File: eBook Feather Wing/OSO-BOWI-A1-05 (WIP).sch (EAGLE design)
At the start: 97 parts, among them IC1 MCP23008/SO, IC2 23K256-I/SN, J1 SJ-43514-SMT, Q1 IRLML0100, SW1 SPDT_SWITCH

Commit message: wing: new footprint for inductor
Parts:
- L1: device microbuilder:INDUCTORNR401 -> Adafruit 3.5in 480x320 FeatherWing:MICROBUILDER_INDUCTORNR401_BIGPADS
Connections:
- net +3V3: now also L1.1; no longer L1.2
- net N$3: now also L1.2; no longer L1.1
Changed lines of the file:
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@@
 <part name="C9" library="microbuilder" deviceset="CAP_CERAMIC" device="0805-NOOUTLINE" value="4.7uF/25V"/>
 <part name="D3" library="microbuilder" deviceset="DIODE-SCHOTTKY" device="SOD-123" value="MBR0530"/>
-<part name="L1" library="microbuilder" deviceset="INDUCTOR" device="NR401" value="10uH"/>
 <part name="R5" library="microbuilder" deviceset="RESISTOR" device="0805_10MGAP" value="0.47ohm"/>
 <part name="U$10" library="microbuilder" deviceset="GND" device=""/>
@@
 <part name="BTN_RESET" library="adafruit" deviceset="SWITCH_PUSHBUTTON" device="C&amp;K_KSS"/>
 <part name="BTN_LOCK" library="adafruit" deviceset="SWITCH_PUSHBUTTON" device="C&amp;K_KSS"/>
+<part name="L1" library="Adafruit 3.5in 480x320 FeatherWing" deviceset="MICROBUILDER_INDUCTOR" device="NR401_BIGPADS" value="10uH"/>
 </parts>
 <sheets>
@@
 <attribute name="VALUE" x="104.1" y="144.78" size="1.27" layer="96" rot="MR270" align="center"/>
 </instance>
-<instance part="L1" gate="G$1" x="83.82" y="149.86" smashed="yes" rot="MR0">
-<attribute name="NAME" x="83.82" y="152.4" size="1.27" layer="95" rot="MR0" align="center"/>
-<attribute name="VALUE" x="83.82" y="148.32" size="1.27" layer="96" rot="MR0" align="center"/>
-</instance>
 <instance part="R5" gate="G$1" x="91.44" y="121.92" smashed="yes" rot="MR270">
 <attribute name="NAME" x="88.9" y="121.92" size="1.27" layer="95" font="vector" rot="MR270" align="center"/>
@@
 <attribute name="NAME" x="233.68" y="105.156" size="1.27" layer="95"/>
 <attribute name="VALUE" x="233.68" y="99.314" size="1.27" layer="96"/>
+</instance>
+<instance part="L1" gate="G$1" x="83.82" y="149.86" smashed="yes">
+<attribute name="NAME" x="83.82" y="152.4" size="1.27" layer="95" align="center"/>
+<attribute name="VALUE" x="83.82" y="148.32" size="1.27" layer="96" align="center"/>
 </instance>
 </instances>
@@
 </segment>
 <segment>
-<pinref part="L1" gate="G$1" pin="2"/>
 <wire x1="76.2" y1="154.94" x2="76.2" y2="149.86" width="0.1524" layer="91"/>
 <wire x1="76.2" y1="149.86" x2="78.74" y2="149.86" width="0.1524" layer="91"/>
 <pinref part="+3V7" gate="G$1" pin="+3V3"/>
+<pinref part="L1" gate="G$1" pin="1"/>
 </segment>
 <segment>
@@
 <wire x1="91.44" y1="149.86" x2="101.6" y2="149.86" width="0.1524" layer="91"/>
 <wire x1="101.6" y1="149.86" x2="101.6" y2="147.32" width="0.1524" layer="91"/>
-<pinref part="L1" gate="G$1" pin="1"/>
 <wire x1="91.44" y1="149.86" x2="88.9" y2="149.86" width="0.1524" layer="91"/>
 <junction x="91.44" y="149.86"/>
@@
 <pinref part="C9" gate="G$1" pin="1"/>
 <wire x1="114.3" y1="149.86" x2="114.3" y2="144.78" width="0.1524" layer="91"/>
-</segment>
-</net>
+<pinref part="L1" gate="G$1" pin="2"/>
+</segment>
+</net>

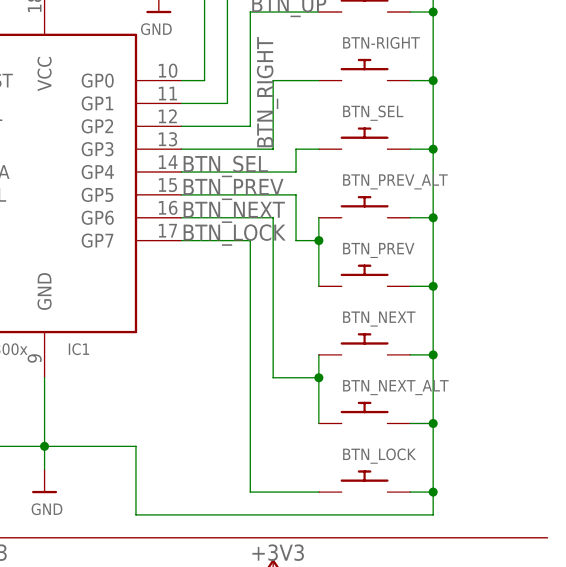
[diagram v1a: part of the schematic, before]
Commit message: rename alt buttons DNP
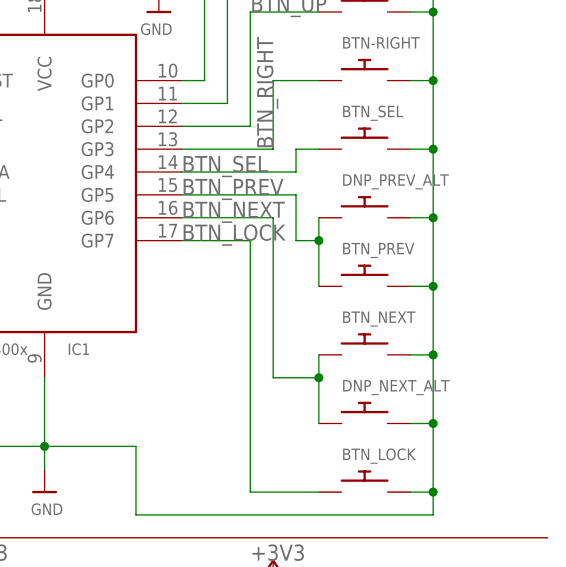
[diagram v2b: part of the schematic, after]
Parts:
- renumbered BTN_NEXT_ALT to DNP_NEXT_ALT, BTN_PREV_ALT to DNP_PREV_ALT
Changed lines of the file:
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@@
 <part name="U$16" library="microbuilder" deviceset="GND" device=""/>
 <part name="U$12" library="microbuilder" deviceset="GND" device=""/>
-<part name="BTN_PREV_ALT" library="My Stuff" deviceset="SPST_TACTILE_SWITCH" device="RA"/>
+<part name="DNP_PREV_ALT" library="My Stuff" deviceset="SPST_TACTILE_SWITCH" device="RA"/>
 <part name="+3V6" library="supply1" library_urn="urn:adsk.eagle:library:371" deviceset="+3V3" device=""/>
 <part name="R4" library="microbuilder" deviceset="RESISTOR" device="_0805MP" value="10K"/>
@@
 <part name="INT" library="Adafruit 3.5in 480x320 FeatherWing" deviceset="MICROBUILDER_SOLDERJUMPER_CLOSED" device=""/>
 <part name="C5" library="microbuilder" deviceset="CAP_CERAMIC" device="0805_10MGAP" value="1uF"/>
-<part name="BTN_NEXT_ALT" library="My Stuff" deviceset="SPST_TACTILE_SWITCH" device="RA"/>
+<part name="DNP_NEXT_ALT" library="My Stuff" deviceset="SPST_TACTILE_SWITCH" device="RA"/>
 <part name="ERST" library="Adafruit 3.5in 480x320 FeatherWing" deviceset="MICROBUILDER_SOLDERJUMPER_CLOSED" device=""/>
 <part name="EBSY" library="Adafruit 3.5in 480x320 FeatherWing" deviceset="MICROBUILDER_SOLDERJUMPER_CLOSED" device=""/>
@@
 <attribute name="VALUE" x="252.984" y="27.94" size="1.27" layer="96" rot="MR0"/>
 </instance>
-<instance part="BTN_PREV_ALT" gate="G$1" x="236.22" y="132.08" smashed="yes">
+<instance part="DNP_PREV_ALT" gate="G$1" x="236.22" y="132.08" smashed="yes">
 <attribute name="NAME" x="233.68" y="135.636" size="1.27" layer="95"/>
 </instance>
@@
 <attribute name="VALUE" x="177.56" y="118.09" size="1.27" layer="96" font="vector" rot="R90" align="center"/>
 </instance>
-<instance part="BTN_NEXT_ALT" gate="G$1" x="236.22" y="109.22" smashed="yes">
+<instance part="DNP_NEXT_ALT" gate="G$1" x="236.22" y="109.22" smashed="yes">
 <attribute name="NAME" x="233.68" y="112.776" size="1.27" layer="95"/>
 </instance>
@@
 <junction x="243.84" y="139.7"/>
 <wire x1="243.84" y1="132.08" x2="243.84" y2="139.7" width="0.1524" layer="91"/>
-<pinref part="BTN_PREV_ALT" gate="G$1" pin="P$2"/>
+<pinref part="DNP_PREV_ALT" gate="G$1" pin="P$2"/>
 <wire x1="241.3" y1="132.08" x2="243.84" y2="132.08" width="0.1524" layer="91"/>
 <junction x="243.84" y="132.08"/>
@@
 <junction x="243.84" y="116.84"/>
 <wire x1="243.84" y1="109.22" x2="243.84" y2="116.84" width="0.1524" layer="91"/>
-<pinref part="BTN_NEXT_ALT" gate="G$1" pin="P$2"/>
+<pinref part="DNP_NEXT_ALT" gate="G$1" pin="P$2"/>
 <wire x1="241.3" y1="109.22" x2="243.84" y2="109.22" width="0.1524" layer="91"/>
 <wire x1="241.3" y1="101.6" x2="243.84" y2="101.6" width="0.1524" layer="91"/>
@@
 <wire x1="226.06" y1="114.3" x2="231.14" y2="114.3" width="0.1524" layer="91"/>
 <wire x1="231.14" y1="114.3" x2="231.14" y2="116.84" width="0.1524" layer="91"/>
-<pinref part="BTN_NEXT_ALT" gate="G$1" pin="P$1"/>
+<pinref part="DNP_NEXT_ALT" gate="G$1" pin="P$1"/>
 <wire x1="231.14" y1="109.22" x2="231.14" y2="114.3" width="0.1524" layer="91"/>
 <junction x="231.14" y="114.3"/>
@@
 <net name="BTN_PREV" class="0">
 <segment>
-<pinref part="BTN_PREV_ALT" gate="G$1" pin="P$1"/>
+<pinref part="DNP_PREV_ALT" gate="G$1" pin="P$1"/>
 <pinref part="IC1" gate="G$1" pin="GP5"/>
 <wire x1="231.14" y1="124.46" x2="231.14" y2="129.54" width="0.1524" layer="91"/>

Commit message: wing: minor silkscreen and routing tweaks
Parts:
- renumbered FCS to BCS
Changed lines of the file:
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@@
 <part name="FID6" library="microbuilder" deviceset="FIDUCIAL" device="_1MM"/>
 <part name="SW1" library="My Stuff" deviceset="SPDT_SWITCH" device=""/>
-<part name="FCS" library="E-Book Wing Rev C (WIP)" deviceset="SOLDERJUMPER_OPEN" device=""/>
+<part name="BCS" library="E-Book Wing Rev C (WIP)" deviceset="SOLDERJUMPER_OPEN" device=""/>
 <part name="J1" library="SJ-43514-SMT" deviceset="SJ-43514-SMT" device=""/>
 <part name="BTN_LEFT" library="adafruit" deviceset="SWITCH_PUSHBUTTON" device="EVQ-PE"/>
@@
 <attribute name="VALUE" x="234.696" y="32.258" size="1.778" layer="96" font="vector" align="top-center"/>
 </instance>
-<instance part="FCS" gate="G$1" x="96.52" y="50.8" smashed="yes"/>
+<instance part="BCS" gate="G$1" x="96.52" y="50.8" smashed="yes"/>
 <instance part="J1" gate="G$1" x="53.34" y="83.82" smashed="yes">
 <attribute name="NAME" x="45.702309375" y="92.22145" size="1.78213125" layer="95"/>
@@
 <wire x1="88.9" y1="50.8" x2="91.44" y2="50.8" width="0.1524" layer="91"/>
 <label x="91.44" y="50.8" size="1.778" layer="95"/>
-<pinref part="FCS" gate="G$1" pin="1"/>
+<pinref part="BCS" gate="G$1" pin="1"/>
 </segment>
 </net>
@@
 <wire x1="101.6" y1="50.8" x2="114.3" y2="50.8" width="0.1524" layer="91"/>
 <label x="101.6" y="50.8" size="1.778" layer="95"/>
-<pinref part="FCS" gate="G$1" pin="2"/>
-</segment>
-</net>
+<pinref part="BCS" gate="G$1" pin="2"/>
+</segment>
+</net>

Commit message: silkscreen updates to e-book wing
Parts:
- MS1: value MICROBUILDER_FEATHERWING_SMTDUAL -> MICROBUILDER_FEATHERWING_SMTDUAL_NOLINES; device My Stuff:MICROBUILDER_FEATHERWING_SMTDUAL -> My Stuff:MICROBUILDER_FEATHERWING_SMTDUAL_NOLINES
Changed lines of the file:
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@@
 <parts>
 <part name="U$2" library="My Stuff" deviceset="WAVESHARE_4_2_INCH_EINK_DISPLAY" device=""/>
-<part name="MS1" library="My Stuff" deviceset="MICROBUILDER_FEATHERWING" device="_SMTDUAL"/>
+<part name="MS1" library="My Stuff" deviceset="MICROBUILDER_FEATHERWING" device="_SMTDUAL_NOLINES" value="MICROBUILDER_FEATHERWING_SMTDUAL_NOLINES"/>
 <part name="MICROSD" library="adafruit" library_urn="urn:adsk.eagle:library:420" deviceset="MICROSD" device="" package3d_urn="urn:adsk.eagle:package:6240723/1"/>
 <part name="GND2" library="supply1" library_urn="urn:adsk.eagle:library:371" deviceset="GND" device=""/>
